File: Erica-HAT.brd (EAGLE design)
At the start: 65 x 56 mm, 64 parts, among them IC1 MEGA8-AI, K1 PIN20X2, Q1 12M, Q2 2.5A/30V, U1 EEPROM24, U2 TMP102, U3 AD5241BRZ1M, U4 MMDT2907A-7-F, U5 +12v

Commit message: Added USB to serial for debug
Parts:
- added CN3: (no value), adafruit:USB-MINIB
- added IC2: FT232RL, ftdichip:SSOP28
- added LED3, LED4: (no value), adafruit:CHIP-LED0603
- added R22, R23: 330R, SparkFun-Passives:0603-RES
- moved U$3 25.6 mm to (29.6, 27.5)
- moved LED2 0.50 mm to (34.0, 27.9)
- moved R16 0.50 mm to (34.0, 24.8)
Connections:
- new net N$44: LED3.A, R22.1
- new net N$45: CN3.D-, IC2.16
- new net N$47: CN3.D+, IC2.15
- new net N$48: LED4.A, R23.1
- new net N$49: IC2.23, LED3.C
- new net N$50: IC2.22, LED4.C
- new net N$51: CN3.VBUS, IC2.20, R22.2, R23.2
- net +3V3: now also IC2.4
- net GND: now also CN3.GND, IC2.18, IC2.21, IC2.25, IC2.26, IC2.7
- net RXD0: now also IC2.1
- net TXD0: now also IC2.5
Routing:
- net RXD0: track 0.00 -> 131.9 mm, vias 0 -> 1
- net TXD0: track 0.00 -> 121.5 mm, vias 0 -> 1
- net +3V3: track 127.0 -> 150.7 mm
- net N$51: track 0.00 -> 19.6 mm
- net N$45: track 0.00 -> 17.1 mm
- net N$47: track 0.00 -> 17.1 mm
- net N$50: track 0.00 -> 13.5 mm
- net N$49: track 0.00 -> 9.22 mm
- net N$2: track 40.9 -> 36.1 mm
- net N$48: track 0.00 -> 1.40 mm
- net N$44: track 0.00 -> 1.40 mm
- net N$30: track 65.8 -> 66.7 mm
- net GND: vias 12 -> 32

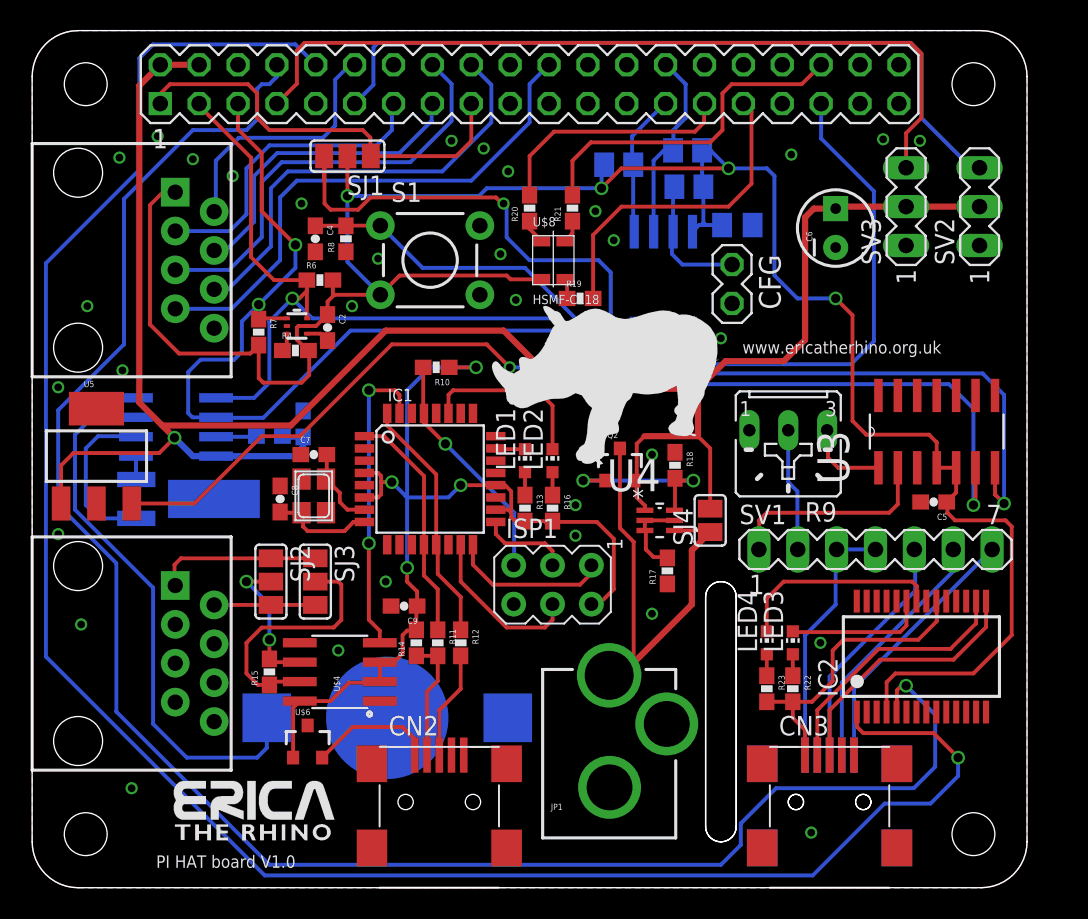
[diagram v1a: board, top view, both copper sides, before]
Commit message: Added silkscreen labels
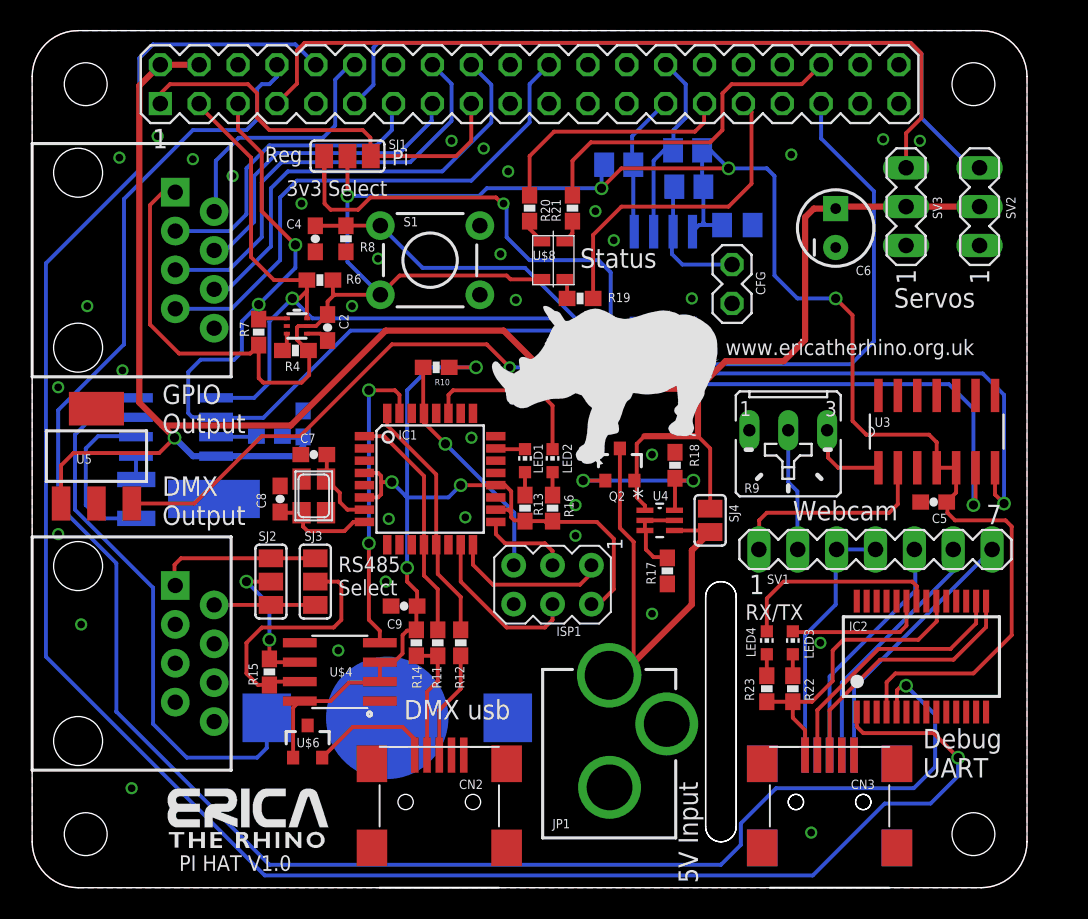
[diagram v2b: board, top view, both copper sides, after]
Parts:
- moved U$2 0.64 mm to (8.10, 2.20)
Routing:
- net GND: vias 32 -> 35
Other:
- board text added: "3v3 Select"
- board text added: "5V Input"
- board text added: "CR1225 or similar"
- board text added: "DMX Output"
- board text added: "DMX usb"
- board text added: "Debug UART"
- board text added: "GPIO Output"
- board text added: "PI HAT V1.0"
- board text added: "Pi"
- board text added: "RS485 Select"
- board text added: "RX/TX"
- board text added: "Reg"
- board text added: "Servos"
- board text added: "Status"
- board text added: "Webcam"
- board text added: "Webcam USB"
- board text removed: "PI HAT board V1.0"

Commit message: Added more stitching vias. Hackvana DRC rules pass.
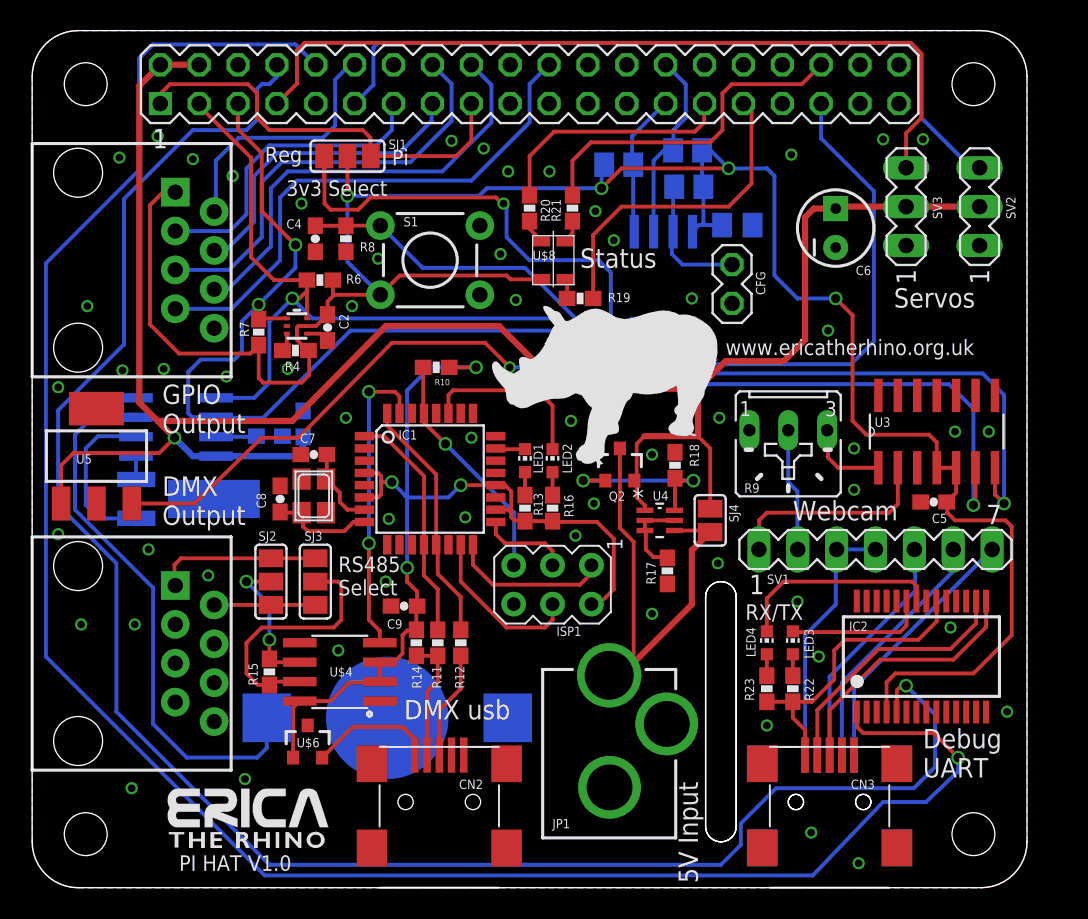
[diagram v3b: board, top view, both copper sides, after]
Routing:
- net GND: vias 35 -> 57
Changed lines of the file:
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@@
 <?xml version="1.0" encoding="utf-8"?>
 <!DOCTYPE eagle SYSTEM "eagle.dtd">
-<eagle version="6.5.0">
+<eagle version="6.6.0">
 <drawing>
 <settings>
@@
 <contactref element="JP1" pad="GNDBREAK"/>
 <contactref element="JP1" pad="GND"/>
-<via x="51.5" y="16" extent="1-16" drill="0.5"/>
+<via x="51.4" y="15.1" extent="1-16" drill="0.5"/>
 <via x="40.5" y="17.9" extent="1-16" drill="0.5"/>
 <via x="40.5" y="28.3" extent="1-16" drill="0.5"/>
@@
 <via x="30.6" y="41.4" extent="1-16" drill="0.5"/>
 <via x="6.5" y="6.5" extent="1-16" drill="0.5"/>
-<via x="35.5" y="25" extent="1-16" drill="0.5"/>
+<via x="36.7" y="25.1" extent="1-16" drill="0.5"/>
 <via x="20.9" y="38" extent="1-16" drill="0.5"/>
 <contactref element="IC2" pad="25"/>
@@
 <via x="10.5" y="47.6" extent="1-16" drill="0.5"/>
 <via x="5.9" y="33.8" extent="1-16" drill="0.5"/>
-<via x="58" y="48.8" extent="1-16" drill="0.5"/>
+<via x="58.2" y="48.9" extent="1-16" drill="0.5"/>
 <via x="55.6" y="48.9" extent="1-16" drill="0.5"/>
 <via x="49.6" y="47.9" extent="1-16" drill="0.5"/>
@@
 <via x="28.3" y="24.2" extent="1-16" drill="0.5"/>
 <via x="28.7" y="29.4" extent="1-16" drill="0.5"/>
+<via x="13.9" y="7.1" extent="1-16" drill="0.5"/>
+<via x="60" y="17" extent="1-16" drill="0.5"/>
+<via x="63.7" y="11.5" extent="1-16" drill="0.5"/>
+<via x="53.7" y="26" extent="1-16" drill="0.5"/>
+<via x="44.8" y="21.2" extent="1-16" drill="0.5"/>
+<via x="50" y="18.7" extent="1-16" drill="0.5"/>
+<via x="48" y="10.6" extent="1-16" drill="0.5"/>
+<via x="54" y="1.6" extent="1-16" drill="0.5"/>
+<via x="60.3" y="29.8" extent="1-16" drill="0.5"/>
+<via x="62.5" y="29.8" extent="1-16" drill="0.5"/>
+<via x="33.8" y="46.8" extent="1-16" drill="0.5"/>
+<via x="20.5" y="30.7" extent="1-16" drill="0.5"/>
+<via x="7.6" y="22.1" extent="1-16" drill="0.5"/>
+<via x="8.6" y="33.9" extent="1-16" drill="0.5"/>
+<via x="6.7" y="17.2" extent="1-16" drill="0.5"/>
+<via x="35.2" y="30.5" extent="1-16" drill="0.5"/>
+<via x="44.9" y="30.7" extent="1-16" drill="0.5"/>
+<via x="52" y="36.4" extent="1-16" drill="0.5"/>
+<via x="12.7" y="33.4" extent="1-16" drill="0.5"/>
+<via x="16.7" y="33.9" extent="1-16" drill="0.5"/>
+<via x="11.5" y="20.4" extent="1-16" drill="0.5"/>
+<via x="53.7" y="28.7" extent="1-16" drill="0.5"/>
 </signal>
 <signal name="+3V3">
@@
 <wire x1="8.37" y1="53.77" x2="7" y2="52.4" width="0.4064" layer="1"/>
 <wire x1="7" y1="52.4" x2="7" y2="31.7" width="0.4064" layer="1"/>
-<wire x1="7" y1="31.7" x2="8.5" y2="30.2" width="0.4064" layer="1"/>
+<wire x1="7" y1="31.7" x2="8.2" y2="30.5" width="0.4064" layer="1"/>
 <via x="9.3" y="29.4" extent="1-16" drill="0.6"/>
-<wire x1="8.5" y1="30.2" x2="9.3" y2="29.4" width="0.4064" layer="1"/>
+<wire x1="8.2" y1="30.5" x2="9.3" y2="29.4" width="0.4064" layer="1"/>
 <wire x1="9.3" y1="29.4" x2="10.505" y2="28.195" width="0.4064" layer="16"/>
 <wire x1="10.505" y1="28.195" x2="12.0162" y2="28.195" width="0.4064" layer="16"/>
@@
 <wire x1="17.7" y1="28.8" x2="17.7" y2="29.45" width="0.4064" layer="16"/>
 <wire x1="43.5" y1="32.6" x2="34.6" y2="32.6" width="0.4064" layer="1"/>
-<wire x1="34.6" y1="32.6" x2="30.8" y2="36.4" width="0.4064" layer="1"/>
-<wire x1="30.8" y1="36.4" x2="23.1" y2="36.4" width="0.4064" layer="1"/>
-<wire x1="23.1" y1="36.4" x2="16.9" y2="30.2" width="0.4064" layer="1"/>
-<wire x1="16.9" y1="30.2" x2="8.5" y2="30.2" width="0.4064" layer="1"/>
+<wire x1="34.6" y1="32.6" x2="30.5" y2="36.7" width="0.4064" layer="1"/>
+<wire x1="30.5" y1="36.7" x2="23.1" y2="36.7" width="0.4064" layer="1"/>
+<wire x1="23.1" y1="36.7" x2="17" y2="30.5" width="0.4064" layer="1"/>
+<wire x1="17" y1="30.5" x2="8.2" y2="30.5" width="0.4064" layer="1"/>
 <wire x1="43.5" y1="32.6" x2="43.5" y2="29.5" width="0.4064" layer="1"/>
 <wire x1="8.37" y1="53.77" x2="10.91" y2="53.77" width="0.4064" layer="1"/>
@@
 <wire x1="22" y1="17.5" x2="22" y2="22.5" width="0.254" layer="1"/>
 <via x="22" y="22.5" extent="1-16" drill="0.6"/>
-<wire x1="22" y1="22.5" x2="22" y2="32.5" width="0.254" layer="16"/>
-<via x="22" y="32.5" extent="1-16" drill="0.6"/>
-<wire x1="22" y1="32.5" x2="23.7" y2="32.5" width="0.254" layer="1"/>
-<wire x1="23.7" y1="32.5" x2="24" y2="32.2" width="0.254" layer="1"/>
-<wire x1="24" y1="32.2" x2="24" y2="30.9926" width="0.254" layer="1"/>
+<wire x1="22" y1="22.5" x2="22" y2="32.4" width="0.254" layer="16"/>
+<via x="22" y="32.4" extent="1-16" drill="0.6"/>
+<wire x1="22" y1="32.4" x2="23.7" y2="32.4" width="0.254" layer="1"/>
+<wire x1="23.7" y1="32.4" x2="24" y2="32.1" width="0.254" layer="1"/>
+<wire x1="24" y1="32.1" x2="24" y2="30.9926" width="0.254" layer="1"/>
 </signal>
 <signal name="N$30">
@@
 <wire x1="58.9" y1="10.1" x2="60.5" y2="8.5" width="0.254" layer="1"/>
 <via x="60.5" y="8.5" extent="1-16" drill="0.6"/>
-<wire x1="60.5" y1="8.5" x2="60.5" y2="7.3" width="0.254" layer="16"/>
-<wire x1="60.5" y1="7.3" x2="58.7" y2="5.5" width="0.254" layer="16"/>
+<wire x1="60.5" y1="8.5" x2="60.5" y2="7.6" width="0.254" layer="16"/>
+<wire x1="60.5" y1="7.6" x2="58.4" y2="5.6" width="0.254" layer="16"/>
 <wire x1="18.53" y1="53.77" x2="17.2" y2="55.1" width="0.254" layer="16"/>
 <wire x1="17.2" y1="55.1" x2="7.9" y2="55.1" width="0.254" layer="16"/>
@@
 <wire x1="0.9" y1="15.1" x2="15.2" y2="0.8" width="0.254" layer="16"/>
 <wire x1="15.2" y1="0.8" x2="51" y2="0.8" width="0.254" layer="16"/>
-<wire x1="51" y1="0.8" x2="55.7" y2="5.5" width="0.254" layer="16"/>
-<wire x1="55.7" y1="5.5" x2="58.7" y2="5.5" width="0.254" layer="16"/>
+<wire x1="51" y1="0.8" x2="55.6" y2="5.6" width="0.254" layer="16"/>
+<wire x1="55.6" y1="5.6" x2="58.4" y2="5.6" width="0.254" layer="16"/>
 </signal>
 <signal name="GPIO18">
@@
 <wire x1="19.076" y1="47.8" x2="19.076" y2="46.176" width="0.254" layer="1"/>
 <wire x1="6.5114" y1="25.1012" x2="10.6012" y2="25.1012" width="0.254" layer="1"/>
-<wire x1="10.6012" y1="25.1012" x2="15" y2="29.5" width="0.254" layer="1"/>
-<wire x1="15" y1="29.5" x2="17.5" y2="29.5" width="0.254" layer="1"/>
-<wire x1="17.5" y1="29.5" x2="23.5" y2="35.5" width="0.254" layer="1"/>
-<wire x1="23.5" y1="35.5" x2="29.7" y2="35.5" width="0.254" layer="1"/>
-<wire x1="29.7" y1="35.5" x2="31.2" y2="34" width="0.254" layer="1"/>
+<wire x1="10.6012" y1="25.1012" x2="15" y2="29.4" width="0.254" layer="1"/>
+<wire x1="15" y1="29.4" x2="17.4" y2="29.4" width="0.254" layer="1"/>
+<wire x1="17.4" y1="29.4" x2="23.5" y2="35.6" width="0.254" layer="1"/>
+<wire x1="23.5" y1="35.6" x2="29.6" y2="35.6" width="0.254" layer="1"/>
+<wire x1="29.6" y1="35.6" x2="31.2" y2="34" width="0.254" layer="1"/>
 <via x="31.2" y="34" extent="1-16" drill="0.5"/>
 <wire x1="31.2" y1="34" x2="35" y2="34" width="0.254" layer="16"/>
@@
 <wire x1="49.7" y1="11.1" x2="49.7" y2="12.15" width="0.254" layer="1"/>
 <wire x1="49.7" y1="12.15" x2="50.95" y2="12.15" width="0.254" layer="1"/>
-<wire x1="50.95" y1="12.15" x2="52.3" y2="13.5" width="0.254" layer="1"/>
-<wire x1="52.3" y1="13.5" x2="52.3" y2="15.5" width="0.254" layer="1"/>
-<wire x1="52.3" y1="15.5" x2="53" y2="16.2" width="0.254" layer="1"/>
-<wire x1="53" y1="16.2" x2="57.9" y2="16.2" width="0.254" layer="1"/>
+<wire x1="50.95" y1="12.15" x2="52.4" y2="13.6" width="0.254" layer="1"/>
+<wire x1="52.4" y1="13.6" x2="52.4" y2="15.5" width="0.254" layer="1"/>
+<wire x1="52.4" y1="15.5" x2="53.1" y2="16.2" width="0.254" layer="1"/>
+<wire x1="53.1" y1="16.2" x2="57.9" y2="16.2" width="0.254" layer="1"/>
 <wire x1="57.9" y1="16.2" x2="59.1" y2="17.4" width="0.254" layer="1"/>
 <wire x1="59.1" y1="17.4" x2="59.1" y2="18.7" width="0.254" layer="1"/>

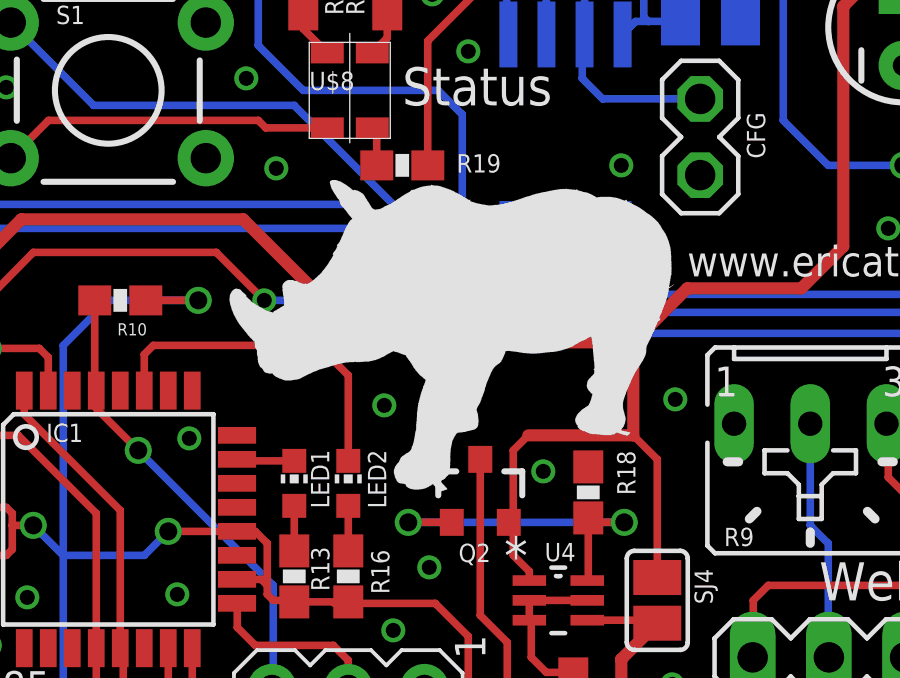
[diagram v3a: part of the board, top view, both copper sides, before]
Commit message: changes for cam output
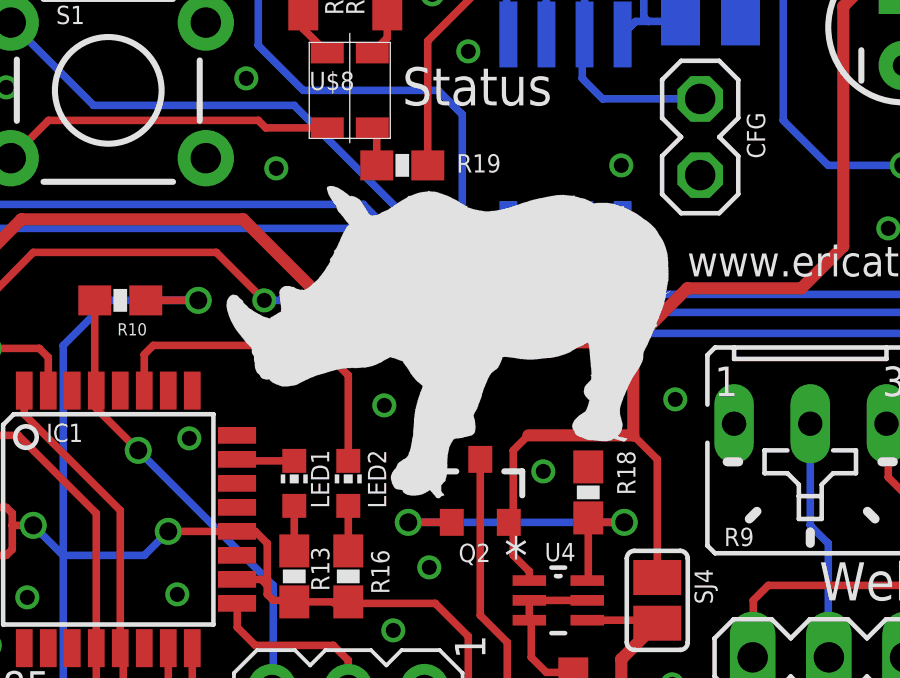
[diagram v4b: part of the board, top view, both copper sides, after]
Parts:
- moved U$3 0.22 mm to (29.5, 27.3)
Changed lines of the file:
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@@
 <?xml version="1.0" encoding="utf-8"?>
 <!DOCTYPE eagle SYSTEM "eagle.dtd">
-<eagle version="6.6.0">
+<eagle version="6.5.0">
 <drawing>
 <settings>
@@
 <wire x1="46" y1="4" x2="45" y2="3" width="0" layer="20" curve="-90"/>
 <wire x1="44" y1="4" x2="45" y2="3" width="0" layer="20" curve="90"/>
-<text x="9.6" y="1.1" size="1.016" layer="112" font="vector">PI HAT V1.0</text>
-<text x="45.3" y="34.8" size="1.016" layer="112" font="vector">www.ericatherhino.org.uk</text>
+<text x="9.6" y="1.1" size="1.016" layer="25" font="vector">PI HAT V1.0</text>
+<text x="45.3" y="34.8" size="1.016" layer="25" font="vector">www.ericatherhino.org.uk</text>
 <text x="30" y="3.3" size="1.016" layer="22" font="vector" rot="MR0">CR1225 or similar</text>
 <text x="58.5" y="10.4" size="1.27" layer="22" font="vector" rot="MR0">Webcam USB</text>
@@
 </element>
 <element name="U$2" library="silkscreen_ERICA" package="ERICA_LOGO" value="ERICALOGO" x="8.1" y="2.2"/>
-<element name="U$3" library="silkscreen_ERICA" package="ERICA_SILHOUETTE" value="ERICASILHOUETTE" x="29.6" y="27.5"/>
+<element name="U$3" library="silkscreen_ERICA" package="ERICA_SILHOUETTE" value="ERICASILHOUETTE" x="29.5" y="27.3"/>
 <element name="U3" library="onecall" package="SOIC127P600X175-14N" value="AD5241BRZ1M" x="59.1" y="29.8" smashed="yes" rot="R90">
 <attribute name="PACKAGE" value="14-Lead SOIC_N" x="59.1" y="29.8" size="1.778" layer="27" rot="R90" display="off"/>
